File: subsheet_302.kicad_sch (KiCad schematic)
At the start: 17 parts, among them J1701 Jumpers, J302 Internal FDD Power, J303 Internal FDD Port, J304 DIN-14S — External FDD Port, U301 WD1772_FLOPPY_DISK_CONTROLLER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, U305 7406_PHY

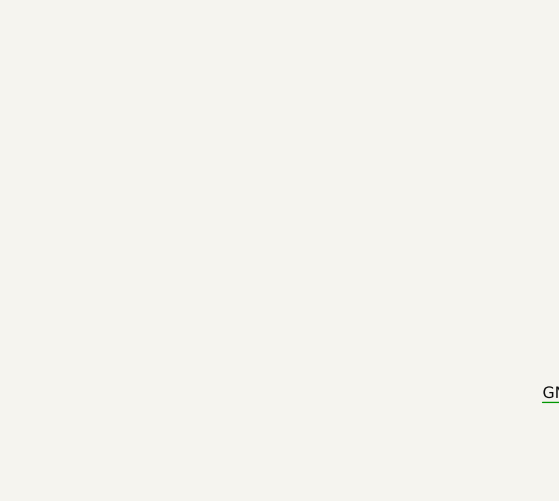
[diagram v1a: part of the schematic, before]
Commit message: add gnd/vcc symbol to start replacing local labels
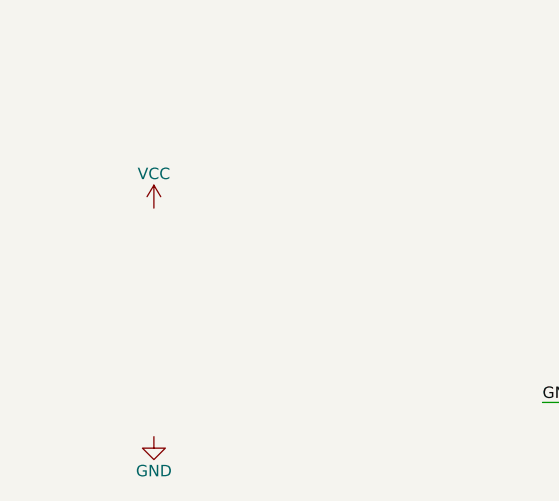
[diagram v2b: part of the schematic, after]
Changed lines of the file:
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@@
     (pin "4")
   )
+  (symbol (lib_id "power:VCC") (at 30.48 214.63 0) (unit 1)
+    (in_bom yes) (on_board yes)
+    (property "Reference" "#PWR?" (id 0) (at 30.48 218.44 0)
+      (effects (font (size 1.27 1.27)) hide)
+    )
+    (property "Value" "VCC" (id 1) (at 30.48 210.82 0))
+    (property "Footprint" "" (id 2) (at 30.48 214.63 0)
+      (effects (font (size 1.27 1.27)) hide)
+    )
+    (property "Datasheet" "" (id 3) (at 30.48 214.63 0)
+      (effects (font (size 1.27 1.27)) hide)
+    )
+    (pin "1")
+  )
+  (symbol (lib_id "power:GND") (at 30.48 240.03 0) (unit 1)
+    (in_bom yes) (on_board yes)
+    (property "Reference" "#PWR?" (id 0) (at 30.48 246.38 0)
+      (effects (font (size 1.27 1.27)) hide)
+    )
+    (property "Value" "GND" (id 1) (at 30.48 243.84 0))
+    (property "Footprint" "" (id 2) (at 30.48 240.03 0)
+      (effects (font (size 1.27 1.27)) hide)
+    )
+    (property "Datasheet" "" (id 3) (at 30.48 240.03 0)
+      (effects (font (size 1.27 1.27)) hide)
+    )
+    (pin "1")
+  )
 )
